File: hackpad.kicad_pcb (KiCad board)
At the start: 2 copper layers, 83.3 x 78.6 mm, 32 parts, among them J1 OLED Connection, SW1 SW_Push, SW11 RotaryEncoder_Switch, SW2 SW_Push, SW3 SW_Push, SW4 SW_Push, SW5 SW_Push, SW6 SW_Push, SW7 SW_Push, SW8 SW_Push

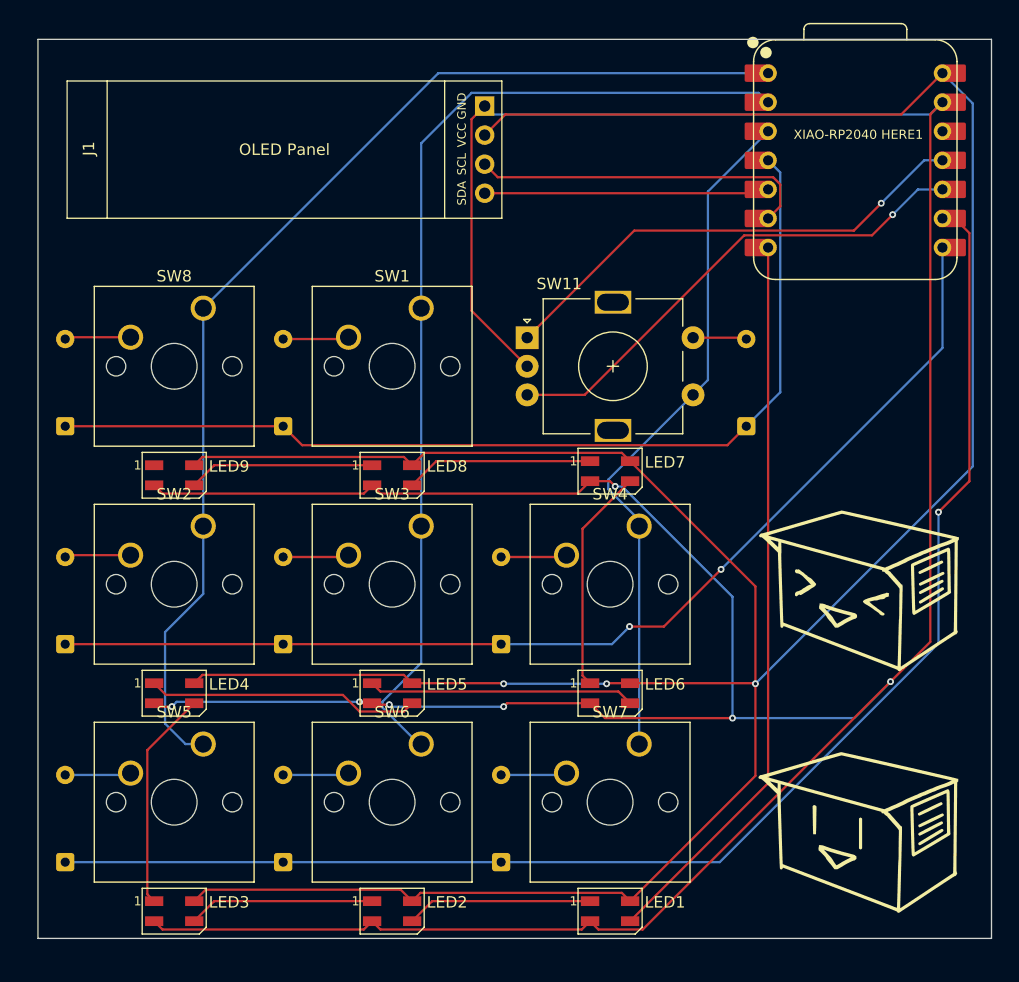
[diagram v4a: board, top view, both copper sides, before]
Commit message: adjust edge cuts and 3D models
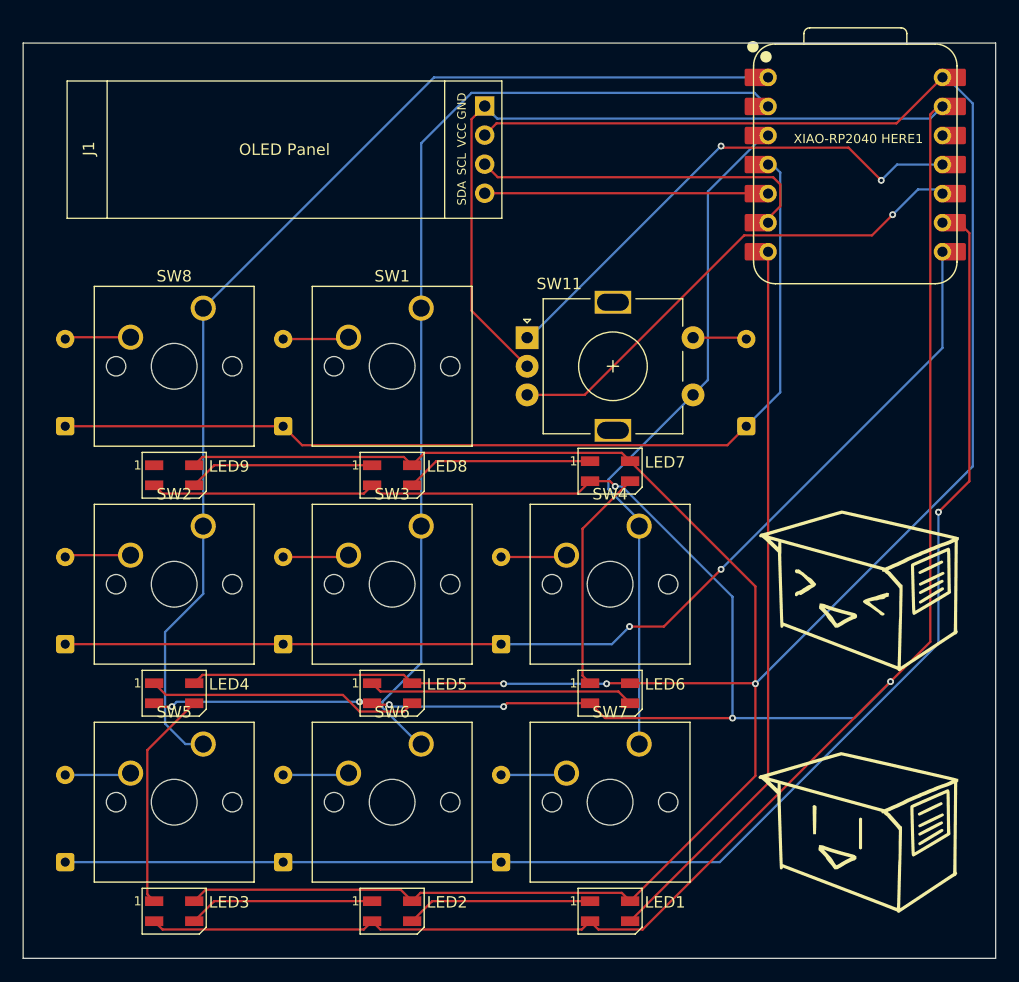
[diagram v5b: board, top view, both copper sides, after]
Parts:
- moved XIAO-RP2040 HERE1 0.37 mm to (135.7, 77.6)
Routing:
- net SW11A: track 42.7 -> 45.1 mm, vias 1 -> 2
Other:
- board size 83.3 x 78.6 mm -> 85 x 80 mm
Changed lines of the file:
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@@
 	(footprint "3D_Model_Footprints:XIAO-RP2040-DIP"
 		(layer "F.Cu")
-		(at 135.73125 77.25)
+		(at 135.73125 77.62)
 		(property "Reference" "XIAO-RP2040 HERE1"
 			(at 0.26875 -2.25 0)
@@
 	)
 	(gr_rect
-		(start 64.29375 66.675)
-		(end 147.6375 145.25625)
+		(start 63 67)
+		(end 148 147)
 		(stroke
 			(width 0.05)
@@
 	)
 	(segment
-		(start 139.74825 73.233)
-		(end 143.35125 69.63)
+		(start 104.368 74.017)
+		(end 139.33425 74.017)
 		(width 0.2)
 		(layer "F.Cu")
@@
 	)
 	(segment
-		(start 103.34 75.045)
-		(end 105.152 73.233)
-		(width 0.2)
-		(layer "F.Cu")
-		(net 12)
-	)
-	(segment
 		(start 114 123)
 		(end 114.05 122.95)
@@
 	)
 	(segment
+		(start 139.33425 74.017)
+		(end 143.35125 70)
+		(width 0.2)
+		(layer "F.Cu")
+		(net 12)
+	)
+	(segment
 		(start 127 131.05)
 		(end 127 123)
@@
 	)
 	(segment
-		(start 105.152 73.233)
-		(end 139.74825 73.233)
+		(start 103.34 75.045)
+		(end 104.368 74.017)
 		(width 0.2)
 		(layer "F.Cu")
@@
 	)
 	(segment
-		(start 103.34 72.505)
-		(end 104.068 73.233)
+		(start 125 126)
+		(end 135.627 126)
 		(width 0.2)
 		(layer "B.Cu")
@@
 	)
 	(segment
-		(start 125 126)
-		(end 135.627 126)
+		(start 103.34 72.505)
+		(end 104.438 73.603)
 		(width 0.2)
 		(layer "B.Cu")
@@
 	)
 	(segment
-		(start 104.068 73.233)
-		(end 142.28825 73.233)
+		(start 104.438 73.603)
+		(end 142.28825 73.603)
 		(width 0.2)
 		(layer "B.Cu")
@@
 	)
 	(segment
-		(start 142.28825 73.233)
-		(end 143.35125 72.17)
+		(start 142.28825 73.603)
+		(end 143.35125 72.54)
 		(width 0.2)
 		(layer "B.Cu")
@@
 	)
 	(segment
-		(start 78.74 90.17)
-		(end 99.28 69.63)
-		(width 0.2)
-		(layer "B.Cu")
-		(net 26)
-	)
-	(segment
 		(start 77.184366 128.27)
 		(end 75.399 126.484634)
@@
 	)
 	(segment
-		(start 99.28 69.63)
-		(end 128.11125 69.63)
+		(start 75.399 126.484634)
+		(end 75.399 118.48253)
 		(width 0.2)
 		(layer "B.Cu")
@@
 	)
 	(segment
-		(start 75.399 126.484634)
-		(end 75.399 118.48253)
+		(start 98.91 70)
+		(end 128.11125 70)
 		(width 0.2)
 		(layer "B.Cu")
@@
 	)
 	(segment
-		(start 75.399 118.48253)
-		(end 78.74 115.14153)
+		(start 78.74 90.17)
+		(end 98.91 70)
 		(width 0.2)
 		(layer "B.Cu")
@@
 	)
 	(segment
-		(start 102.189 71.354)
-		(end 127.29525 71.354)
+		(start 75.399 118.48253)
+		(end 78.74 115.14153)
 		(width 0.2)
 		(layer "B.Cu")
-		(net 27)
+		(net 26)
 	)
 	(segment
-		(start 97.79 75.753)
-		(end 102.189 71.354)
+		(start 97.79 90.17)
+		(end 97.79 75.753)
 		(width 0.2)
 		(layer "B.Cu")
@@
 	)
 	(segment
-		(start 97.79 90.17)
-		(end 97.79 75.753)
+		(start 97.79 75.753)
+		(end 102.189 71.354)
 		(width 0.2)
 		(layer "B.Cu")
@@
 	)
 	(segment
-		(start 127.29525 71.354)
-		(end 128.11125 72.17)
+		(start 102.189 71.354)
+		(end 126.92525 71.354)
+		(width 0.2)
+		(layer "B.Cu")
+		(net 27)
+	)
+	(segment
+		(start 126.92525 71.354)
+		(end 128.11125 72.54)
 		(width 0.2)
 		(layer "B.Cu")
@@
 	)
 	(segment
-		(start 116.407 83.393)
-		(end 135.607 83.393)
+		(start 135.143 76.143)
+		(end 138 79)
 		(width 0.2)
 		(layer "F.Cu")
@@
 	)
 	(segment
-		(start 107.05 92.75)
-		(end 116.407 83.393)
+		(start 124 76)
+		(end 124.143 76.143)
 		(width 0.2)
 		(layer "F.Cu")
@@
 	)
 	(segment
-		(start 135.607 83.393)
-		(end 138 81)
+		(start 124.143 76.143)
+		(end 135.143 76.143)
 		(width 0.2)
 		(layer "F.Cu")
@@
 	)
 	(via
-		(at 138 81)
+		(at 138 79)
 		(size 0.6)
 		(drill 0.3)
@@
 		(net 30)
 	)
+	(via
+		(at 124 76)
+		(size 0.6)
+		(drill 0.3)
+		(layers "F.Cu" "B.Cu")
+		(net 30)
+	)
+	(segment
+		(start 139.38 77.62)
+		(end 143.35125 77.62)
+		(width 0.2)
+		(layer "B.Cu")
+		(net 30)
+	)
+	(segment
+		(start 107.05 92.75)
+		(end 107.25 92.75)
+		(width 0.2)
+		(layer "B.Cu")
+		(net 30)
+	)
 	(segment
-		(start 138 81)
-		(end 141.75 77.25)
+		(start 138 79)
+		(end 139.38 77.62)
 		(width 0.2)
 		(layer "B.Cu")
@@
 	)
 	(segment
-		(start 141.75 77.25)
-		(end 143.35125 77.25)
+		(start 107.25 92.75)
+		(end 124 76)
 		(width 0.2)
 		(layer "B.Cu")

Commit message: make changes according to advice
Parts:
- moved anime 2.02 mm to (128.1, 125.7)
- moved LED7 0.36 mm to (114.3, 104.8)
- turned LED4 to 180 degrees
- turned LED5 to 180 degrees
- turned LED6 to 180 degrees
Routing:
- net GND: track 327.0 -> 21.5 mm, vias 7 -> 4
- net +5V: track 280.7 -> 305.3 mm
- net Column 1: track 88.1 -> 75.7 mm
- net Net-(LED4-DOUT): track 23.9 -> 16.3 mm
- net Net-(LED6-DOUT): track 19.7 -> 26.8 mm, vias 0 -> 2
- net Row 2: track 124.1 -> 117.0 mm, vias 1 -> 0
- net Net-(LED5-DOUT): track 23.3 -> 16.3 mm
- net Column 0: track 99.5 -> 95.8 mm
- net SW11A: track 45.1 -> 42.6 mm, vias 2 -> 0
- net SCL: track 30.0 -> 27.7 mm, vias 0 -> 1
- net LED: track 63.9 -> 65.7 mm, vias 0 -> 2
- net Row 1: track 96.2 -> 94.9 mm, vias 2 -> 0
- net Row 0: track 85.8 -> 87.0 mm
- net Column 2: track 60.5 -> 59.6 mm
- net Net-(LED3-DOUT): track 19.2 -> 20.0 mm
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- added copper zone on B.Cu, net GND
- added copper zone on F.Cu, net GND

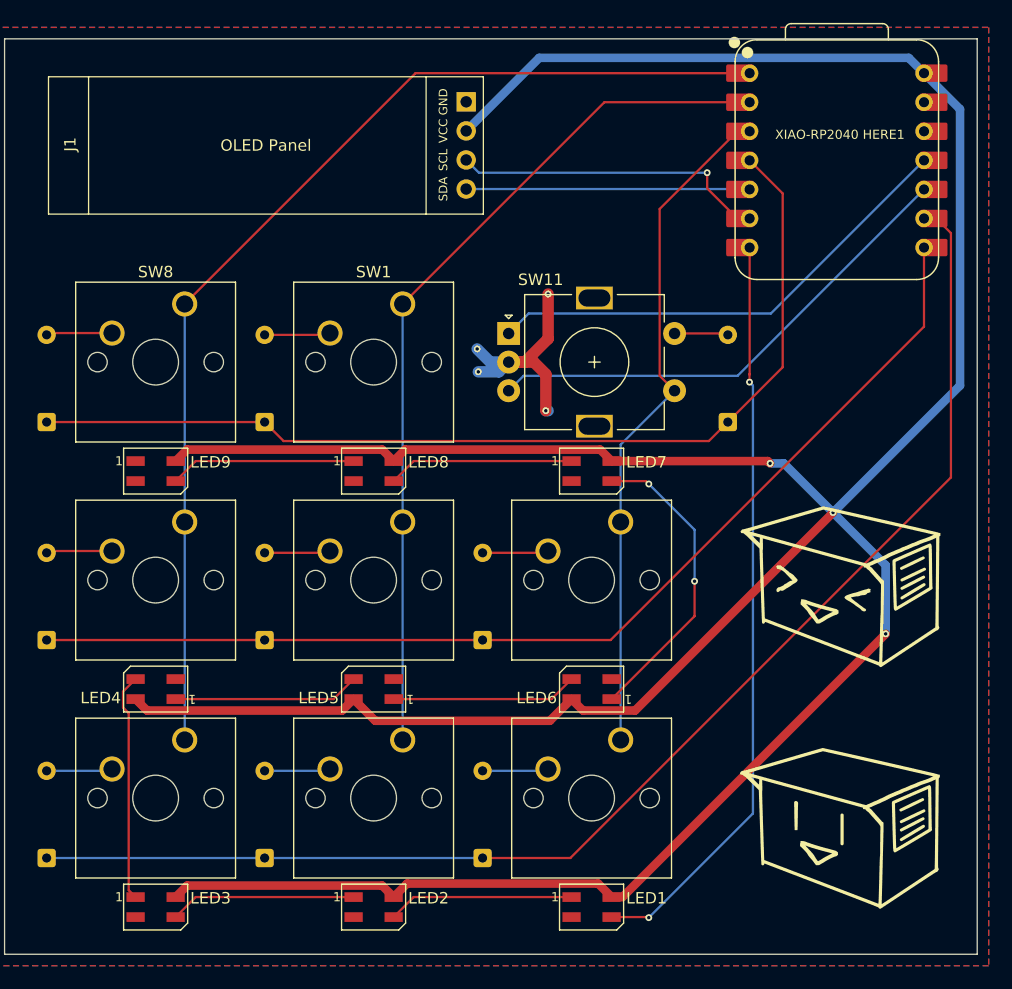
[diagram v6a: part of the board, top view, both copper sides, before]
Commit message: update 3D model of pcb with small adjustments
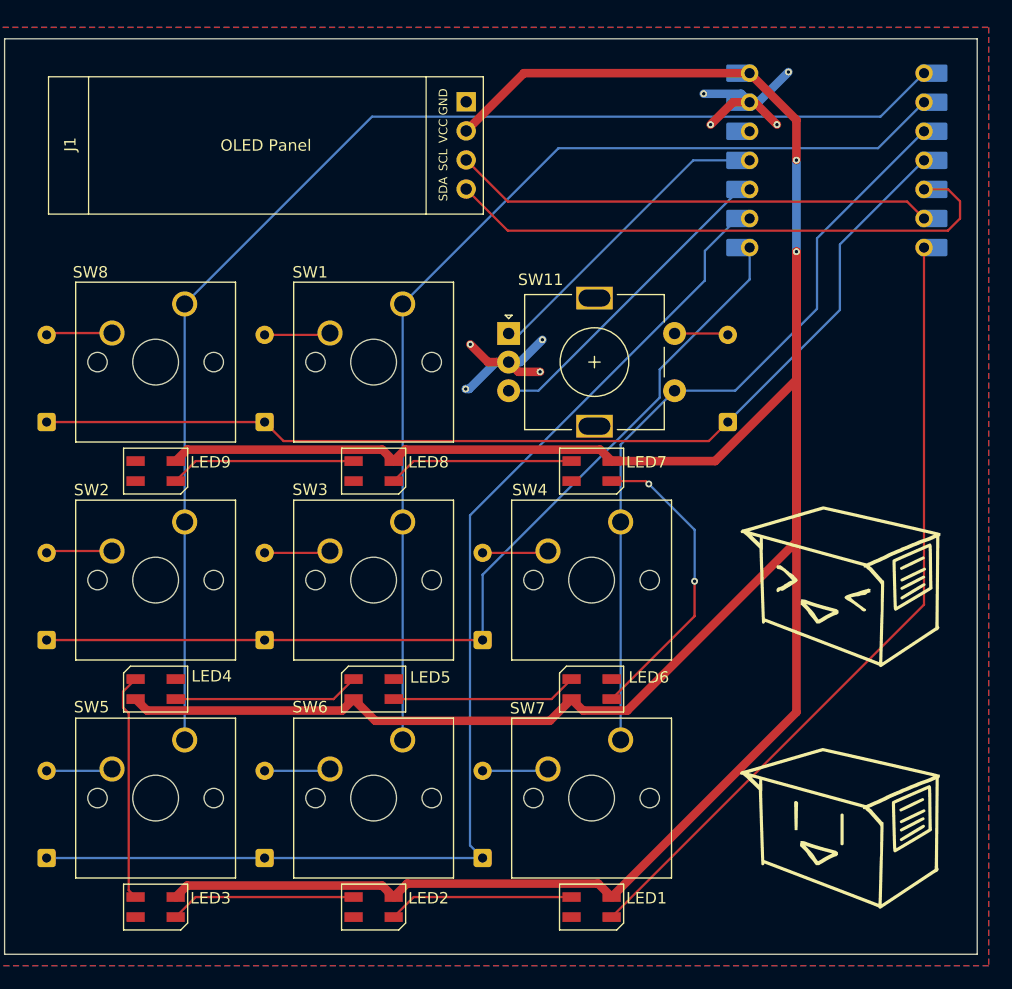
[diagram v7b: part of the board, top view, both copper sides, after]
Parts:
- XIAO-RP2040 HERE1: moved to B.Cu
- turned XIAO-RP2040 HERE1 to 180 degrees
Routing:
- net SDA: track 24.8 -> 50.2 mm
- net SW11B: track 43.6 -> 28.3 mm
- net SW11A: track 42.6 -> 27.3 mm
- net Column 0: track 95.8 -> 111.1 mm
- net Column 1: track 75.7 -> 91.0 mm
- net SCL: track 27.7 -> 42.1 mm, vias 1 -> 0
- net Row 1: track 94.9 -> 82.1 mm
- net Row 2: track 117.0 -> 105.2 mm
- net GND: track 21.5 -> 31.8 mm, vias 4 -> 8
- net Column 2: track 59.6 -> 67.3 mm
- net LED: track 65.7 -> 69.8 mm, vias 2 -> 0
- net Row 0: track 87.0 -> 90.9 mm
- net +5V: track 305.3 -> 309.2 mm, vias 3 -> 2
